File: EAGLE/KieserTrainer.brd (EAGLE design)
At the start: 50.5 x 69.8 mm, 11 parts, among them U1 ATMEGA328P-PU

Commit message: Update schematic to match PCB
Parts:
- removed IC1: (no value), dp_devices:DIL28-N
- removed R3: (no value), rcl:R0805
- added S1: (no value), adafruit:EG1218
- added S2: (no value), adafruit:B3F-40XX
- JP1: value (none) -> +
- JP2: value (none) -> -
- LED1: value (none) -> Blue
- LED2: value (none) -> Red
- R1, R2: value (none) -> 270R
- renumbered SG1 to BUZ
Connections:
- removed net N$6: BUZ.-, R3.1
- new net AVCC: U1.20
- new net N$7: JP1.1, S1.P
- net GND: now also BUZ.-; no longer R3.2
- net N$1: now also U1.11; no longer U1.14
- net VCC: now also S1.S; no longer U1.20
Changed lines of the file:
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@@
 <attribute name="OC_FARNELL" value="1715487" x="1.27" y="8.89" size="1.778" layer="27" rot="R270" display="off"/>
 </element>
-<element name="SG1" library="buzzer" package="F/CM12P" value="F/CM12P" x="25.4" y="58.42" rot="R315">
+<element name="BUZ" library="buzzer" package="F/CM12P" value="F/CM12P" x="25.4" y="58.42" rot="R315">
 <attribute name="OC_NEWARK" value="unknown" x="1.15330625" y="5.436490625" size="1.778" layer="27" rot="R315" display="off"/>
 <attribute name="MPN" value="" x="1.15330625" y="5.436490625" size="1.778" layer="27" rot="R315" display="off"/>
@@
 <attribute name="OC_FARNELL" value="unknown" x="1.15330625" y="5.436490625" size="1.778" layer="27" rot="R315" display="off"/>
 </element>
-<element name="LED1" library="adafruit" package="CHIPLED_0805" value="" x="39.37" y="60.96"/>
-<element name="LED2" library="adafruit" package="CHIPLED_0805" value="" x="11.43" y="60.96"/>
-<element name="R1" library="rcl" package="R0805" value="" x="39.37" y="55.88" rot="R90"/>
-<element name="R2" library="rcl" package="R0805" value="" x="11.43" y="55.88" rot="R270"/>
-<element name="JP1" library="pinhead" package="1X01" value="" x="-40.64" y="48.26"/>
-<element name="JP2" library="pinhead" package="1X01" value="" x="-45.72" y="48.26"/>
-<element name="R3" library="rcl" package="R0805" value="" x="16.51" y="66.04" rot="R180"/>
+<element name="LED1" library="adafruit" package="CHIPLED_0805" value="Blue" x="39.37" y="60.96"/>
+<element name="LED2" library="adafruit" package="CHIPLED_0805" value="Red" x="11.43" y="60.96"/>
+<element name="R1" library="rcl" package="R0805" value="270R" x="39.37" y="55.88" rot="R90"/>
+<element name="R2" library="rcl" package="R0805" value="270R" x="11.43" y="55.88" rot="R270"/>
+<element name="JP1" library="pinhead" package="1X01" value="+" x="-40.64" y="48.26"/>
+<element name="JP2" library="pinhead" package="1X01" value="-" x="-45.72" y="48.26"/>
 <element name="JP3" library="pinhead" package="2X03" value="" x="-52.07" y="5.08"/>
-<element name="IC1" library="dp_devices" package="DIL28-N" value="" x="-35.56" y="-6.35"/>
+<element name="S1" library="adafruit" package="EG1218" value="" x="-49.53" y="-5.08"/>
+<element name="S2" library="adafruit" package="B3F-40XX" value="" x="-46.99" y="-16.51">
+<attribute name="OC_NEWARK" value="36K3105" x="-46.99" y="-16.51" size="1.778" layer="27" display="off"/>
+<attribute name="MPN" value="B3F-4000" x="-46.99" y="-16.51" size="1.778" layer="27" display="off"/>
+<attribute name="MF" value="OMRON COMPONENTS USA" x="-46.99" y="-16.51" size="1.778" layer="27" display="off"/>
+<attribute name="OC_FARNELL" value="176434" x="-46.99" y="-16.51" size="1.778" layer="27" display="off"/>
+</element>
 </elements>
 <signals>
@@
 <contactref element="U1" pad="8"/>
 <contactref element="U1" pad="22"/>
-<contactref element="R3" pad="2"/>
 <contactref element="LED1" pad="C"/>
 <contactref element="LED2" pad="C"/>
 <contactref element="JP3" pad="6"/>
-<wire x1="24.13" y1="48.26" x2="39.37" y2="62.01" width="0" layer="19" extent="1-1"/>
+<contactref element="BUZ" pad="-"/>
+<wire x1="22.705921875" y1="61.114075" x2="39.37" y2="62.01" width="0" layer="19" extent="1-1"/>
+<wire x1="11.43" y1="62.01" x2="22.705921875" y2="61.114075" width="0" layer="19" extent="1-1"/>
+<wire x1="24.13" y1="48.26" x2="22.705921875" y2="61.114075" width="0" layer="19" extent="1-1"/>
 <wire x1="26.67" y1="40.64" x2="24.13" y2="48.26" width="0" layer="19" extent="1-1"/>
-<wire x1="11.43" y1="62.01" x2="24.13" y2="48.26" width="0" layer="19" extent="1-1"/>
-<wire x1="15.56" y1="66.04" x2="11.43" y2="62.01" width="0" layer="19" extent="1-1"/>
 <wire x1="-45.72" y1="48.26" x2="11.43" y2="62.01" width="0" layer="19" extent="1-1"/>
 <wire x1="-49.53" y1="6.35" x2="-45.72" y2="48.26" width="0" layer="19" extent="1-1"/>
@@
 <signal name="VCC">
 <contactref element="U1" pad="7"/>
-<contactref element="U1" pad="20"/>
 <contactref element="JP3" pad="2"/>
-<wire x1="21.59" y1="40.64" x2="26.67" y2="48.26" width="0" layer="19" extent="1-1"/>
-<wire x1="-54.61" y1="6.35" x2="21.59" y2="40.64" width="0" layer="19" extent="1-1"/>
-</signal>
-<signal name="N$6">
-<contactref element="SG1" pad="-"/>
-<contactref element="R3" pad="1"/>
-<wire x1="17.46" y1="66.04" x2="22.705921875" y2="61.114075" width="0" layer="19" extent="1-1"/>
-</signal>
-<signal name="N$1">
-<contactref element="U1" pad="14"/>
-<contactref element="R2" pad="1"/>
-<wire x1="8.89" y1="48.26" x2="11.43" y2="56.83" width="0" layer="19" extent="1-1"/>
+<contactref element="S1" pad="S"/>
+<wire x1="-46.99" y1="-5.08" x2="26.67" y2="48.26" width="0" layer="19" extent="1-1"/>
+<wire x1="-54.61" y1="6.35" x2="-46.99" y2="-5.08" width="0" layer="19" extent="1-1"/>
 </signal>
 <signal name="N$2">
@@
 <signal name="N$5">
 <contactref element="U1" pad="5"/>
-<contactref element="SG1" pad="+"/>
+<contactref element="BUZ" pad="+"/>
 <wire x1="28.094075" y1="55.725921875" x2="31.75" y2="48.26" width="0" layer="19" extent="1-1"/>
 </signal>
+<signal name="N$1">
+<contactref element="U1" pad="11"/>
+<contactref element="R2" pad="1"/>
+<wire x1="16.51" y1="48.26" x2="11.43" y2="56.83" width="0" layer="19" extent="1-1"/>
+</signal>
+<signal name="N$7">
+<contactref element="JP1" pad="1"/>
+<contactref element="S1" pad="P"/>
+<wire x1="-40.64" y1="48.26" x2="-49.53" y2="-5.08" width="0" layer="19" extent="1-1"/>
+</signal>
+<signal name="AVCC">
+<contactref element="U1" pad="20"/>
+</signal>
 </signals>

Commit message: Make both LEDs blue high-power (brighter!), add 2x mystery diode to make ~5V out of ~6V
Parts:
- added D1, D2: (no value), diode:D-7.5
- LED2: value Red -> blue
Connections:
- new net N$6: D1.A, S1.S
- new net N$8: D1.C, D2.A
- net VCC: now also D2.C; no longer S1.S
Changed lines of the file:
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@@
 </element>
 <element name="LED1" library="adafruit" package="CHIPLED_0805" value="Blue" x="39.37" y="60.96"/>
-<element name="LED2" library="adafruit" package="CHIPLED_0805" value="Red" x="11.43" y="60.96"/>
+<element name="LED2" library="adafruit" package="CHIPLED_0805" value="blue" x="11.43" y="60.96"/>
 <element name="R1" library="rcl" package="R0805" value="270R" x="39.37" y="55.88" rot="R90"/>
 <element name="R2" library="rcl" package="R0805" value="270R" x="11.43" y="55.88" rot="R270"/>
@@
 <attribute name="OC_FARNELL" value="176434" x="-46.99" y="-16.51" size="1.778" layer="27" display="off"/>
 </element>
+<element name="D1" library="diode" package="D-7.5" value="" x="-49.53" y="-26.67"/>
+<element name="D2" library="diode" package="D-7.5" value="" x="-49.53" y="-31.75"/>
 </elements>
 <signals>
@@
 <contactref element="U1" pad="7"/>
 <contactref element="JP3" pad="2"/>
-<contactref element="S1" pad="S"/>
-<wire x1="-46.99" y1="-5.08" x2="26.67" y2="48.26" width="0" layer="19" extent="1-1"/>
-<wire x1="-54.61" y1="6.35" x2="-46.99" y2="-5.08" width="0" layer="19" extent="1-1"/>
+<contactref element="D2" pad="C"/>
+<wire x1="-54.61" y1="6.35" x2="-53.34" y2="-31.75" width="0" layer="19" extent="1-1"/>
+<wire x1="26.67" y1="48.26" x2="-54.61" y2="6.35" width="0" layer="19" extent="1-1"/>
 </signal>
 <signal name="N$2">
@@
 <contactref element="U1" pad="20"/>
 </signal>
+<signal name="N$6">
+<contactref element="S1" pad="S"/>
+<contactref element="D1" pad="A"/>
+<wire x1="-46.99" y1="-5.08" x2="-45.72" y2="-26.67" width="0" layer="19" extent="1-1"/>
+</signal>
+<signal name="N$8">
+<contactref element="D1" pad="C"/>
+<contactref element="D2" pad="A"/>
+<wire x1="-45.72" y1="-31.75" x2="-53.34" y2="-26.67" width="0" layer="19" extent="1-1"/>
+</signal>
 </signals>

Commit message: Add bypass capactior on uC supply pins
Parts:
- added C1: 100n, rcl:C0805
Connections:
- net GND: now also C1.2
- net VCC: now also C1.1
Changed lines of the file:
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@@
 <element name="D1" library="diode" package="D-7.5" value="" x="-49.53" y="-26.67"/>
 <element name="D2" library="diode" package="D-7.5" value="" x="-49.53" y="-31.75"/>
+<element name="C1" library="rcl" package="C0805" value="100n" x="-53.34" y="-36.83"/>
 </elements>
 <signals>
@@
 <contactref element="JP3" pad="6"/>
 <contactref element="BUZ" pad="-"/>
+<contactref element="C1" pad="2"/>
 <wire x1="22.705921875" y1="61.114075" x2="39.37" y2="62.01" width="0" layer="19" extent="1-1"/>
 <wire x1="11.43" y1="62.01" x2="22.705921875" y2="61.114075" width="0" layer="19" extent="1-1"/>
@@
 <wire x1="-45.72" y1="48.26" x2="11.43" y2="62.01" width="0" layer="19" extent="1-1"/>
 <wire x1="-49.53" y1="6.35" x2="-45.72" y2="48.26" width="0" layer="19" extent="1-1"/>
+<wire x1="-52.39" y1="-36.83" x2="-49.53" y2="6.35" width="0" layer="19" extent="1-1"/>
 </signal>
 <signal name="VCC">
@@
 <contactref element="JP3" pad="2"/>
 <contactref element="D2" pad="C"/>
+<contactref element="C1" pad="1"/>
+<wire x1="-53.34" y1="-31.75" x2="-54.29" y2="-36.83" width="0" layer="19" extent="1-1"/>
 <wire x1="-54.61" y1="6.35" x2="-53.34" y2="-31.75" width="0" layer="19" extent="1-1"/>
 <wire x1="26.67" y1="48.26" x2="-54.61" y2="6.35" width="0" layer="19" extent="1-1"/>

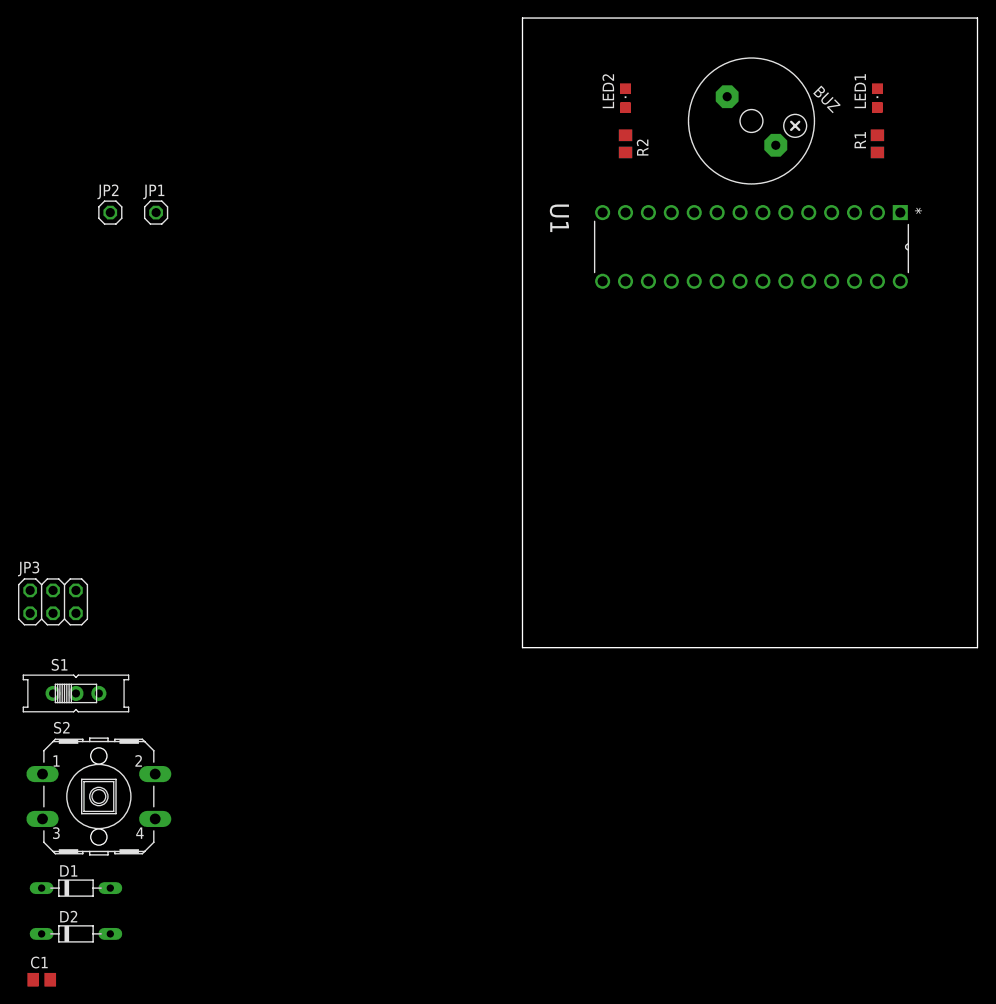
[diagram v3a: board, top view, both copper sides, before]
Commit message: Add board layout to match physical design
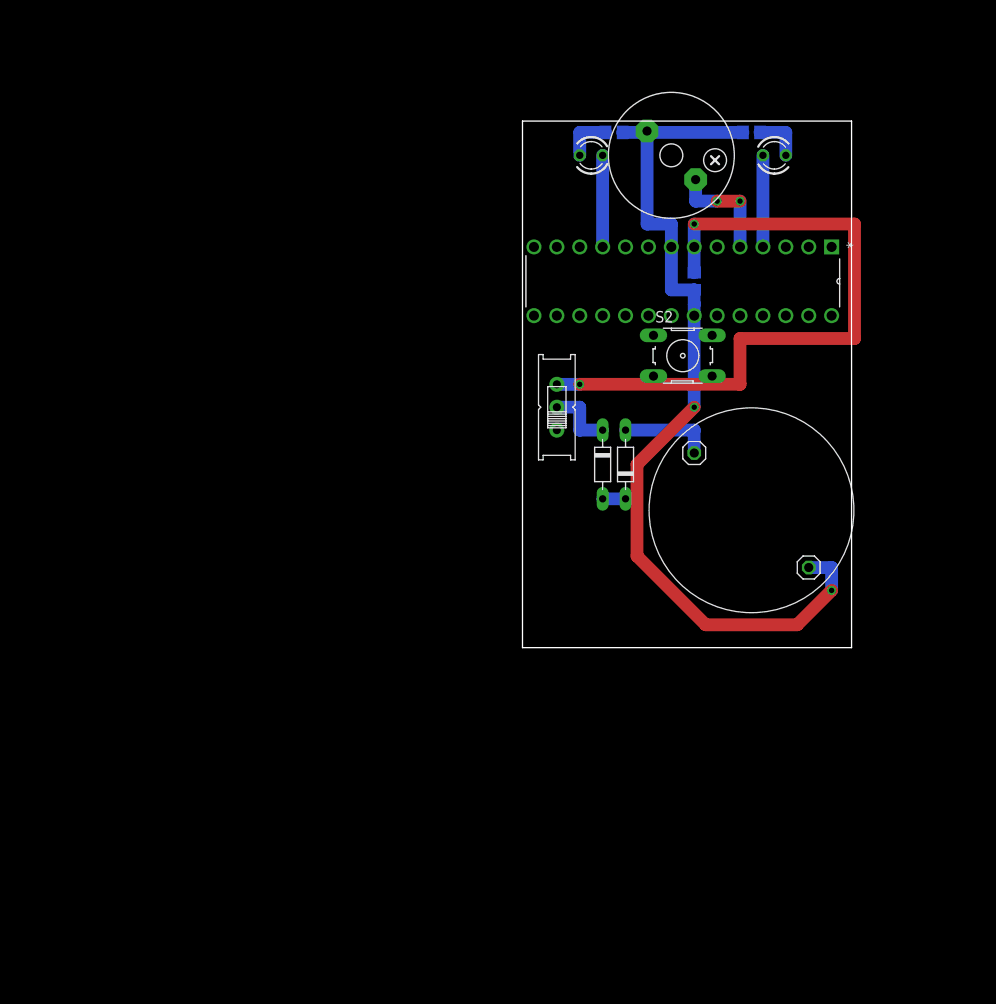
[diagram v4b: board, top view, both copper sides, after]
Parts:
- removed JP3: (no value), pinhead:2X03
- LED1: value Blue -> (none); device adafruit:CHIPLED_0805 -> led:LED3MM
- LED2: value blue -> (none); device adafruit:CHIPLED_0805 -> led:LED3MM
- S2: device adafruit:B3F-40XX -> switch-omron:B3F-10XX
- moved C1 106.0 mm to (19.1, 40.6), flipped to the bottom, turned to 270 degrees
- moved JP2 86.9 mm to (31.8, 8.89)
- moved S2 81.2 mm to (17.8, 32.4)
- moved D2 78.3 mm to (8.89, 20.3), turned to 270 degrees
- moved D1 77.0 mm to (11.4, 20.3), turned to 90 degrees
- moved JP1 65.4 mm to (19.1, 21.6)
- moved S1 62.1 mm to (3.81, 26.7), turned to 90 degrees
- moved R1 14.0 mm to (25.4, 57.1), flipped to the bottom, turned to 0 degrees
- moved LED1 13.1 mm to (27.9, 54.6)
- moved BUZ 9.67 mm to (16.5, 54.6)
- moved U1 8.52 mm to (1.27, 36.8)
- moved LED2 7.41 mm to (7.62, 54.6), turned to 180 degrees
- moved R2 1.80 mm to (10.2, 57.1), flipped to the bottom, turned to 180 degrees
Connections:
- net GND: now also R1.2, R2.2; no longer JP3.6, LED1.C, LED2.C
- net MISO: no longer JP3.1
- net MOSI: no longer JP3.4
- net N$1: now also LED1.K, R1.1; no longer R2.1, U1.11
- net N$2: now also LED2.K, R2.1; no longer LED2.A, R2.2
- net N$3: now also U1.4; no longer R1.2
- net N$4: now also LED2.A, U1.11; no longer R1.1, U1.4
- net N$6: now also JP1.1; no longer S1.S
- net N$7: now also D2.C; no longer JP1.1
- net RST: no longer JP3.5
- net SCK: no longer JP3.3
- net VCC: now also S1.S; no longer D2.C, JP3.2
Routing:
- net GND: track 0.00 -> 99.9 mm, vias 0 -> 2
- net VCC: track 0.00 -> 74.0 mm, vias 0 -> 2
- net N$5: track 0.00 -> 12.4 mm, vias 0 -> 2
- net N$6: track 0.00 -> 10.2 mm
- net N$4: track 0.00 -> 10.2 mm
- net N$3: track 0.00 -> 10.2 mm
- net N$7: track 0.00 -> 7.62 mm
- net N$2: track 0.00 -> 5.40 mm
- net N$1: track 0.00 -> 5.40 mm
- net N$8: track 0.00 -> 2.54 mm
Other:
- board size 50.5 x 69.8 mm -> 36.5 x 58.4 mm

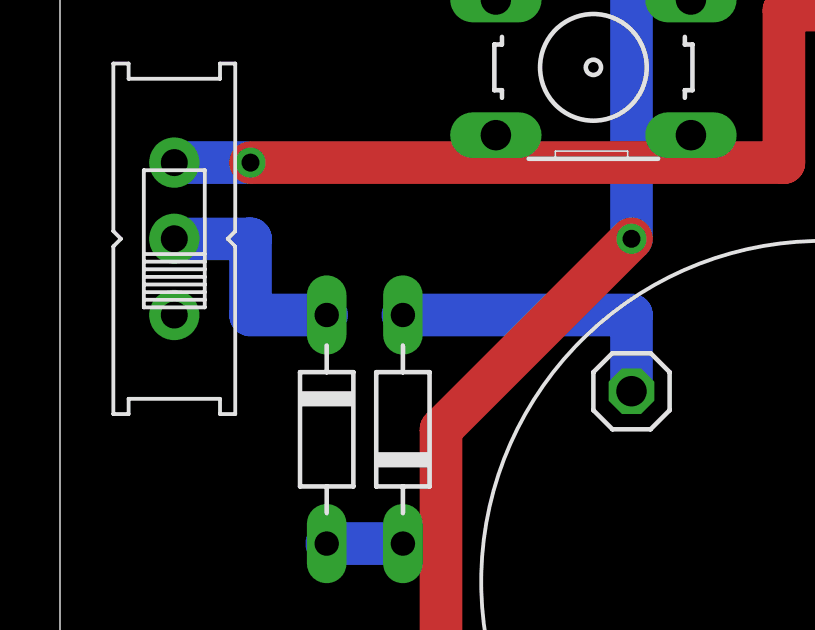
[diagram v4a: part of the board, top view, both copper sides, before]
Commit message: Bypass mystery diodes to feed ATmega with full 6V (exactly the max rating, but oh well)
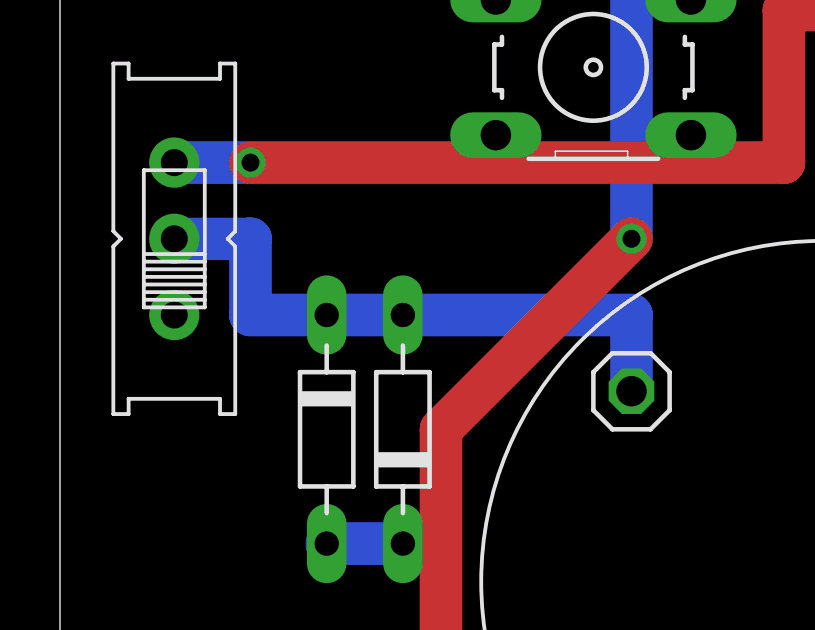
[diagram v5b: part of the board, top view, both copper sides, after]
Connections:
- removed net N$7: D2.C, S1.P
- net N$6: now also D2.C, S1.P
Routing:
- net N$6: track 10.2 -> 20.3 mm
- net N$7: track 7.62 -> 0.00 mm
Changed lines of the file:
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@@
 <wire x1="19.05" y1="21.59" x2="19.05" y2="24.13" width="1.4224" layer="16"/>
 <wire x1="19.05" y1="24.13" x2="11.43" y2="24.13" width="1.4224" layer="16"/>
-</signal>
-<signal name="N$7">
 <contactref element="D2" pad="C"/>
 <contactref element="S1" pad="P"/>
@@
 <wire x1="6.35" y1="26.67" x2="6.35" y2="24.13" width="1.4224" layer="16"/>
 <wire x1="6.35" y1="24.13" x2="8.89" y2="24.13" width="1.4224" layer="16"/>
+<wire x1="11.43" y1="24.13" x2="8.89" y2="24.13" width="1.4224" layer="16"/>
 </signal>
 </signals>
